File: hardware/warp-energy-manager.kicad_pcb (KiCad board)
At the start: 4 copper layers, 68 x 87 mm, 89 parts, among them J101 Boot, P101 CON-SENSOR2, P102 Relay, P103 L+N, P104 OUT, P105 INPUT, P106 DNP, P110 MODBUS, P111 Debug, Q102 SI2305CDS-T1-GE3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

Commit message: changed RS485 resistors
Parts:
- R134, R136: value 2.7k -> 750
- R135: value 2.2k -> DNP
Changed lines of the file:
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@@
       (effects (font (size 0.2 0.2) (thickness 0.05)))
     )
-    (fp_text value 2.7k (at 0.05 -0.375) (layer F.Fab)
+    (fp_text value 750 (at 0.05 -0.375) (layer F.Fab)
       (effects (font (size 0.2 0.2) (thickness 0.05)))
     )
@@
       (effects (font (size 0.2 0.2) (thickness 0.05)))
     )
-    (fp_text value 2.2k (at 0.05 -0.375) (layer F.Fab)
+    (fp_text value DNP (at 0.05 -0.375) (layer F.Fab)
       (effects (font (size 0.2 0.2) (thickness 0.05)))
     )
@@
       (effects (font (size 0.2 0.2) (thickness 0.05)))
     )
-    (fp_text value 2.7k (at 0.05 -0.375) (layer F.Fab)
+    (fp_text value 750 (at 0.05 -0.375) (layer F.Fab)
       (effects (font (size 0.2 0.2) (thickness 0.05)))
     )

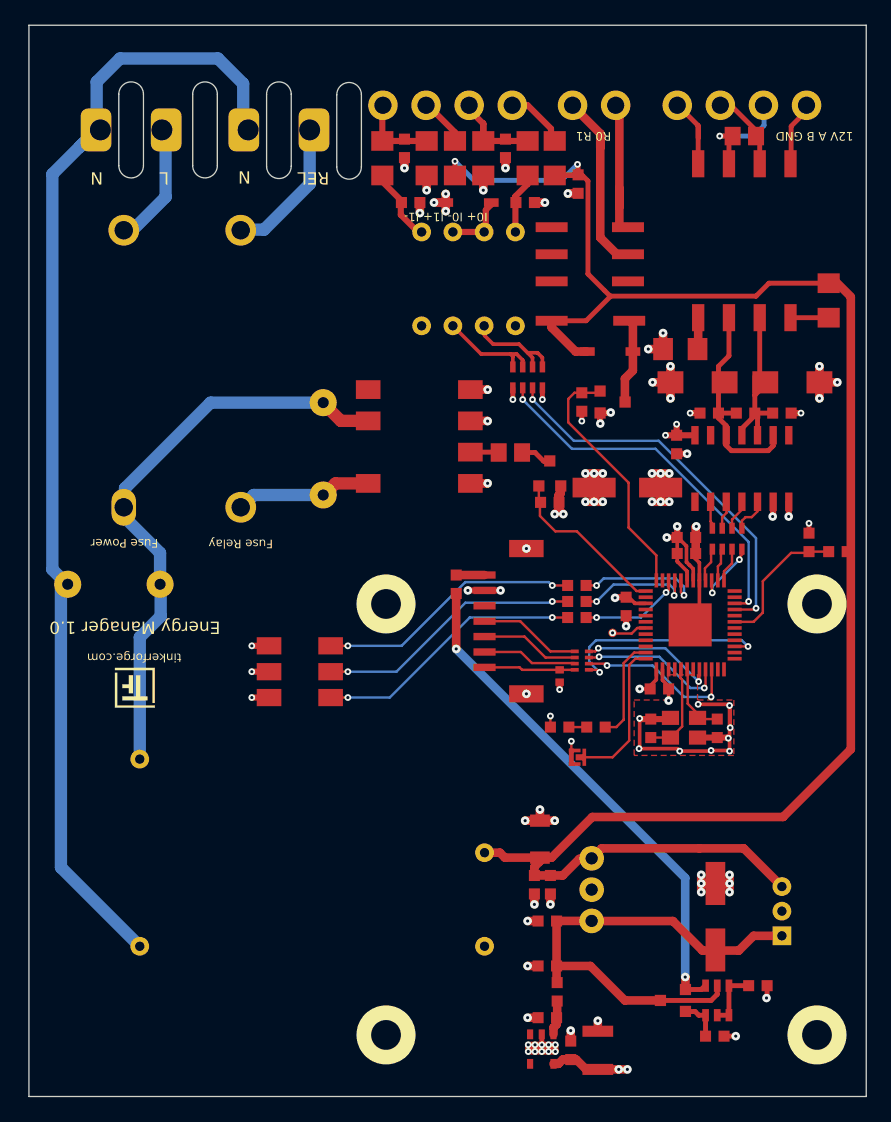
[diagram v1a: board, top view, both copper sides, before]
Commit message: version 1.1
 * fix relay pinning
 * fix ac/dc power supply position
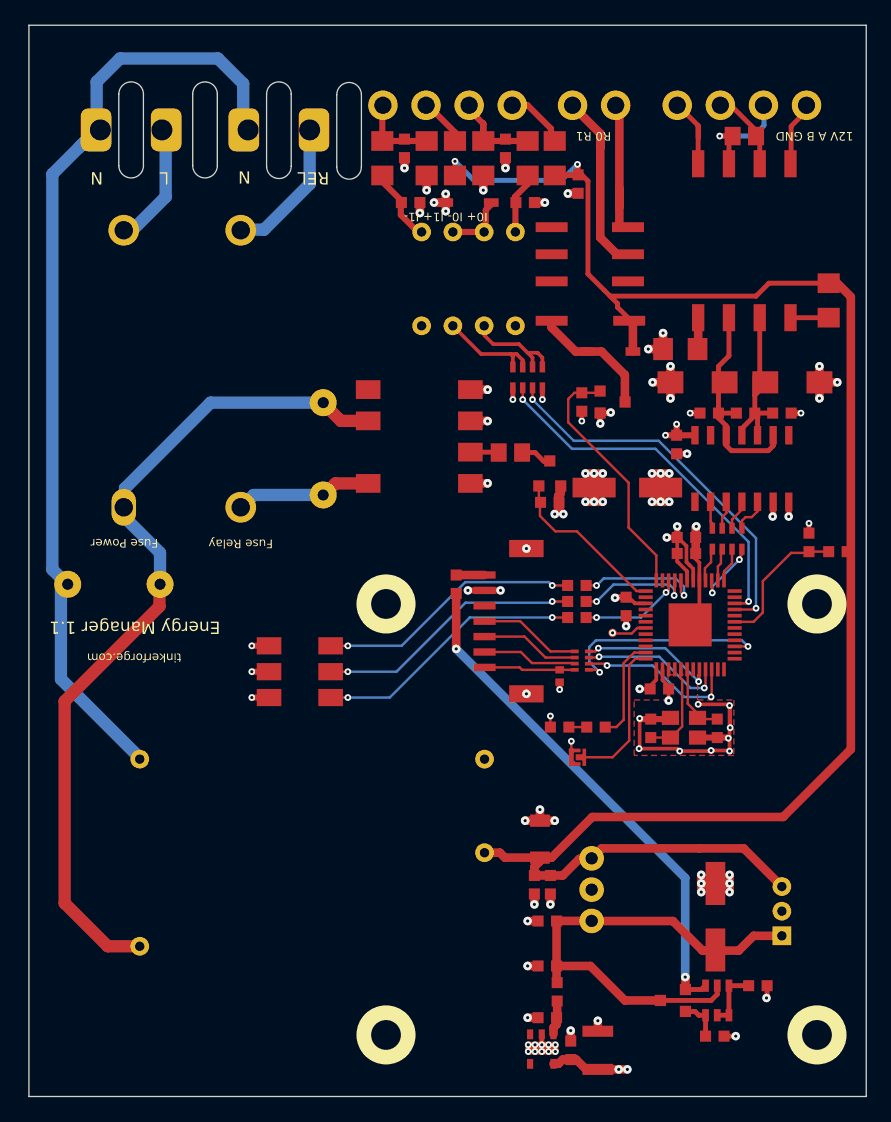
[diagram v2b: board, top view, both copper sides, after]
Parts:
- removed G***: LOGO, kicad-libraries:Logo_31x31
- R134, R136: value 750 -> 2.7k
- R135: value DNP -> 2.2k
- U111: moved to F.Cu
- turned D107 to 0 degrees
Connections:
- REL101 pad 1: Net-(D107-Pad1) -> VCC
- REL101 pad 8: VCC -> Net-(D107-Pad1)
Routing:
- net L: track 47.6 -> 69.4 mm
- net N: track 94.1 -> 78.8 mm
- net VCC: track 152.2 -> 147.8 mm
- net Net-(D107-Pad1): track 7.16 -> 10.3 mm
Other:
- board text added: "Energy Manager 1.1"
- board text removed: "Energy Manager 1.0"

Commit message: enlarged esp holes
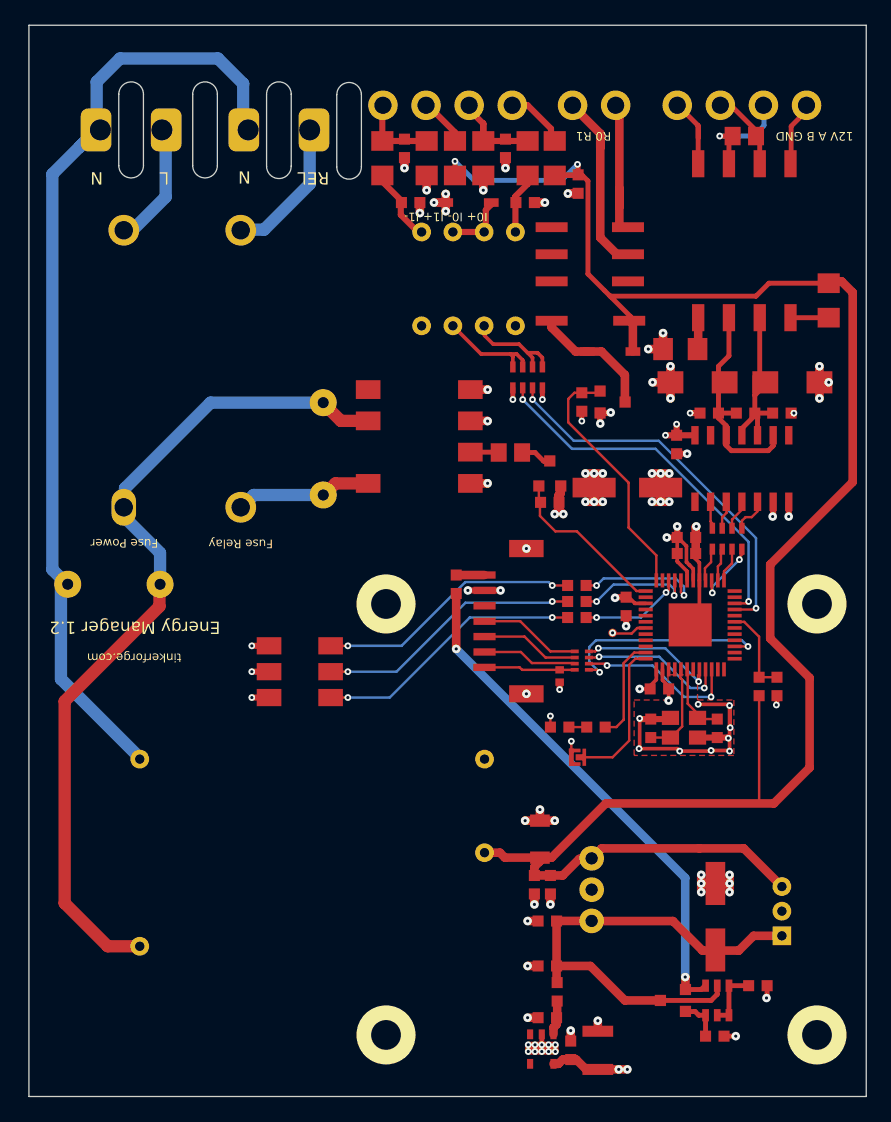
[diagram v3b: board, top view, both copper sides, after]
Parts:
- moved R107 12.7 mm to (151.7, 105.2), turned to 270 degrees
- moved R108 12.0 mm to (153.1, 105.2), turned to 90 degrees
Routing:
- net VCC: track 147.8 -> 158.5 mm
- net V12: track 11.7 -> 7.28 mm
- net GND: track 105.0 -> 103.7 mm
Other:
- board text added: "Energy Manager 1.2"
- board text removed: "Energy Manager 1.1"

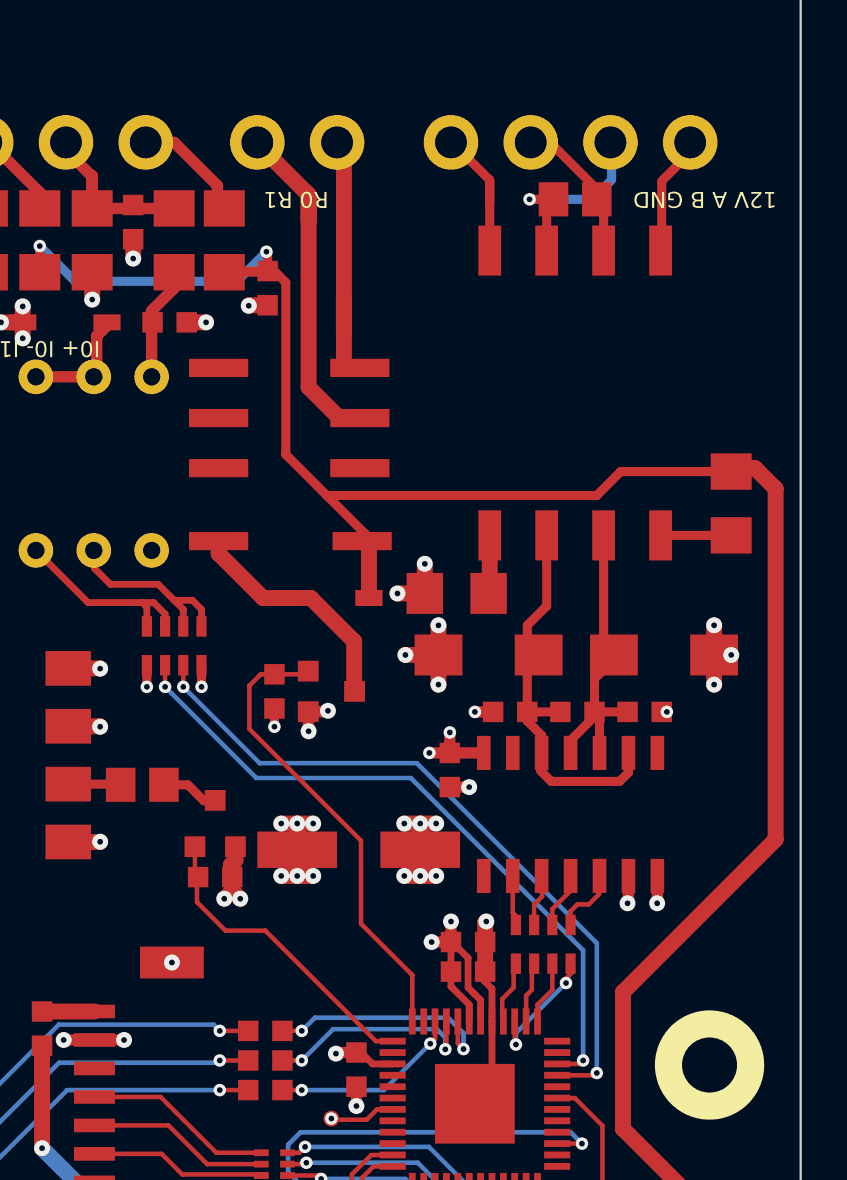
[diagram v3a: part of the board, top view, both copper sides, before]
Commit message: finish version 1.2
 * move elko
 * change rs485 resistors
 * design improvements
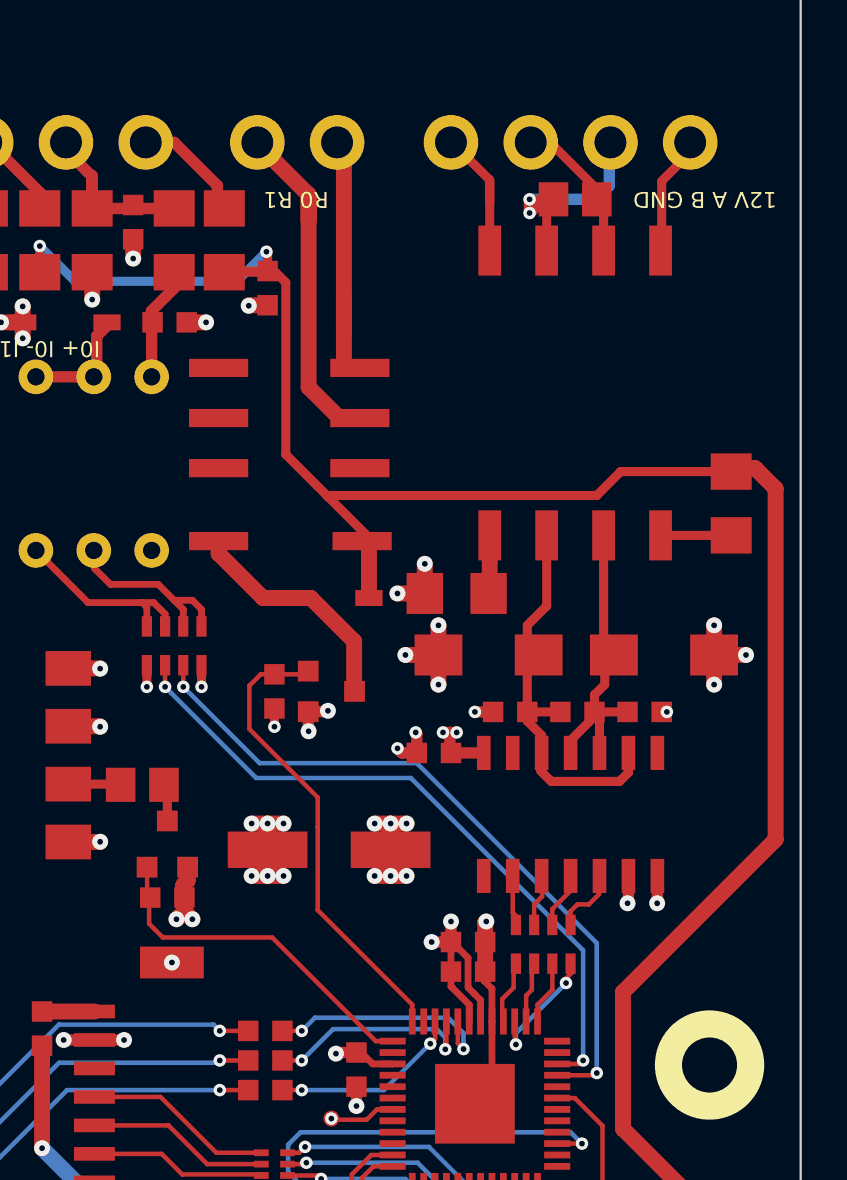
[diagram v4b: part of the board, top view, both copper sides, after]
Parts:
- A101, A102, A103, A104: footprint kicad-libraries:DRILL_NP -> kicad-libraries:DRILL_NP_35
- R134, R136: value 2.7k -> 750
- R135: value 2.2k -> DNP
- moved R115 2.28 mm to (132.6, 91.2)
- moved Q102 2.28 mm to (132.6, 88.8)
- moved C109 1.30 mm to (139.7, 89.1)
- moved C132 1.03 mm to (144.2, 84.8), turned to 0 degrees
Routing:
- net Net-(L104-Pad7): track 9.30 -> 15.0 mm, vias 1 -> 2
- net RELAY: track 13.7 -> 15.5 mm
- net GND: track 103.7 -> 105.4 mm, vias 81 -> 82
- net Net-(D106-Pad1): track 15.4 -> 13.9 mm
- net Net-(Q102-PadD): track 2.54 -> 1.70 mm
- net 3V3: track 70.8 -> 71.5 mm

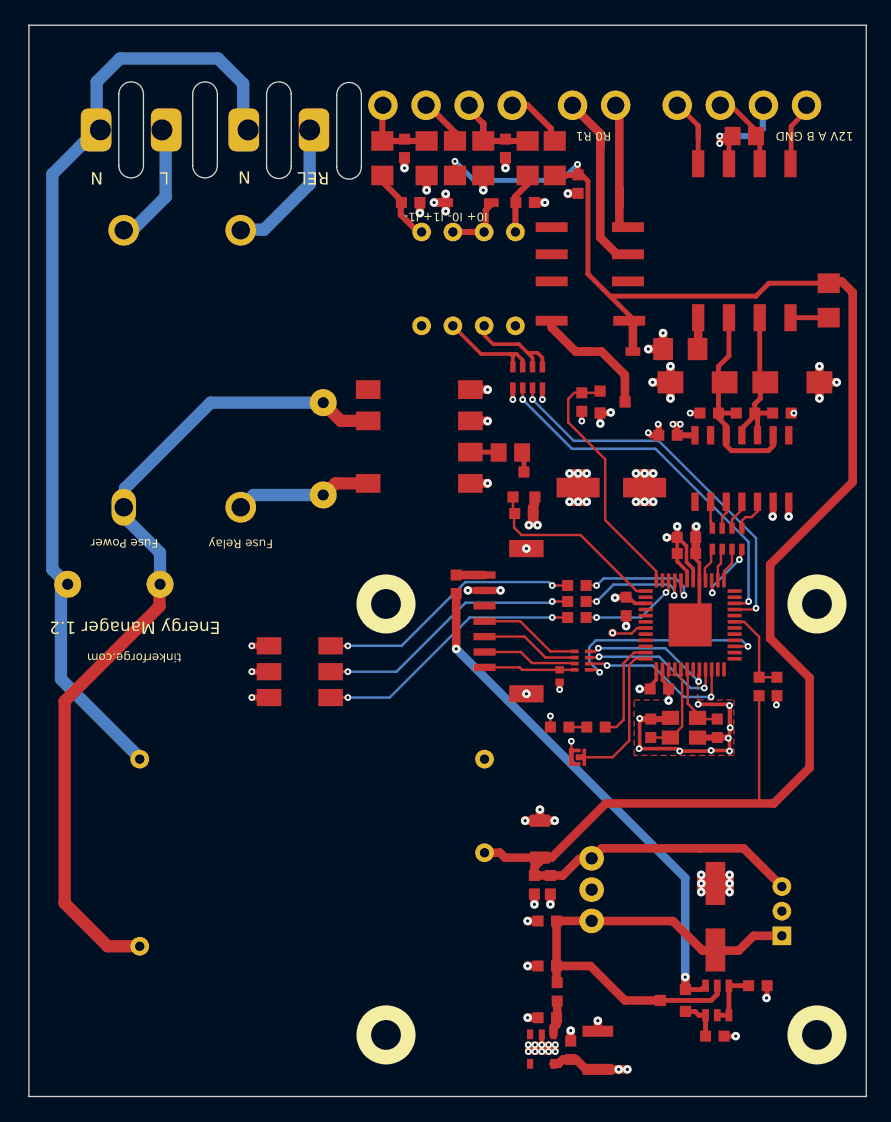
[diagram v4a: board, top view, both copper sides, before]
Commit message: add version 1.3
 * add 12V output for rs485
 * change protection diodes type
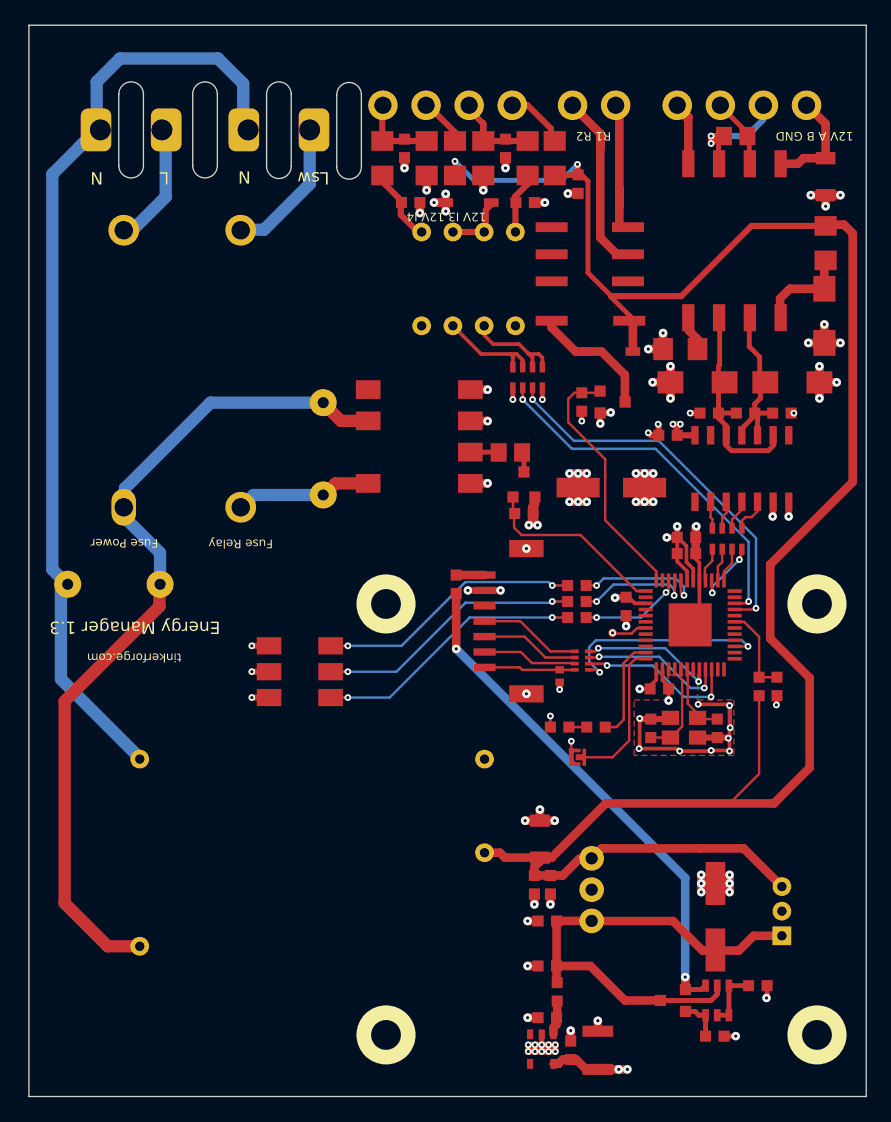
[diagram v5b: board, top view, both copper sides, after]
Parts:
- added C115: 4.7uF/50V, kicad-libraries:C1206, F.Cu at (157.1, 63.9)
- added D102: SMAJ12CA, DO-214AC, F.Cu at (156.9, 75.2)
- D106, D111: value SMAJ24CA -> SMAJ12CA
- PTC102: value DNP -> PTC 0.45A
- moved PTC102 4.66 mm to (157.1, 69.2)
- moved L104 0.80 mm to (149.7, 69.0)
- moved R137 0.70 mm to (149.8, 60.5)
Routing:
- net VCC: track 158.5 -> 166.6 mm
- net GND: track 105.4 -> 112.8 mm, vias 82 -> 88
- net Net-(D102-Pad2): track 3.10 -> 8.05 mm
- net Net-(L104-Pad8): track 6.98 -> 10.2 mm
- net Net-(C115-Pad2): track 6.02 -> 8.66 mm
- net Net-(D106-Pad1): track 13.9 -> 15.0 mm
- net Net-(D111-Pad1): track 18.0 -> 18.5 mm
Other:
- board text added: "12V I3 12V I4"
- board text added: "Energy Manager 1.3"
- board text added: "Lsw"
- board text added: "R1 R2"
- board text removed: "Energy Manager 1.2"
- board text removed: "I0+ I0- I1+ I1-"
- board text removed: "R0 R1"
- board text removed: "REL"
